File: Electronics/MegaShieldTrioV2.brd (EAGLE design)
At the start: 99.8 x 80 mm, 37 parts, among them X1 Vehicle control, X2 2odo__, X3 1odo__, X4 RJ45-8L-B, X5 S5B-ZR, X6 S6B-ZR, X7 22-23-2031

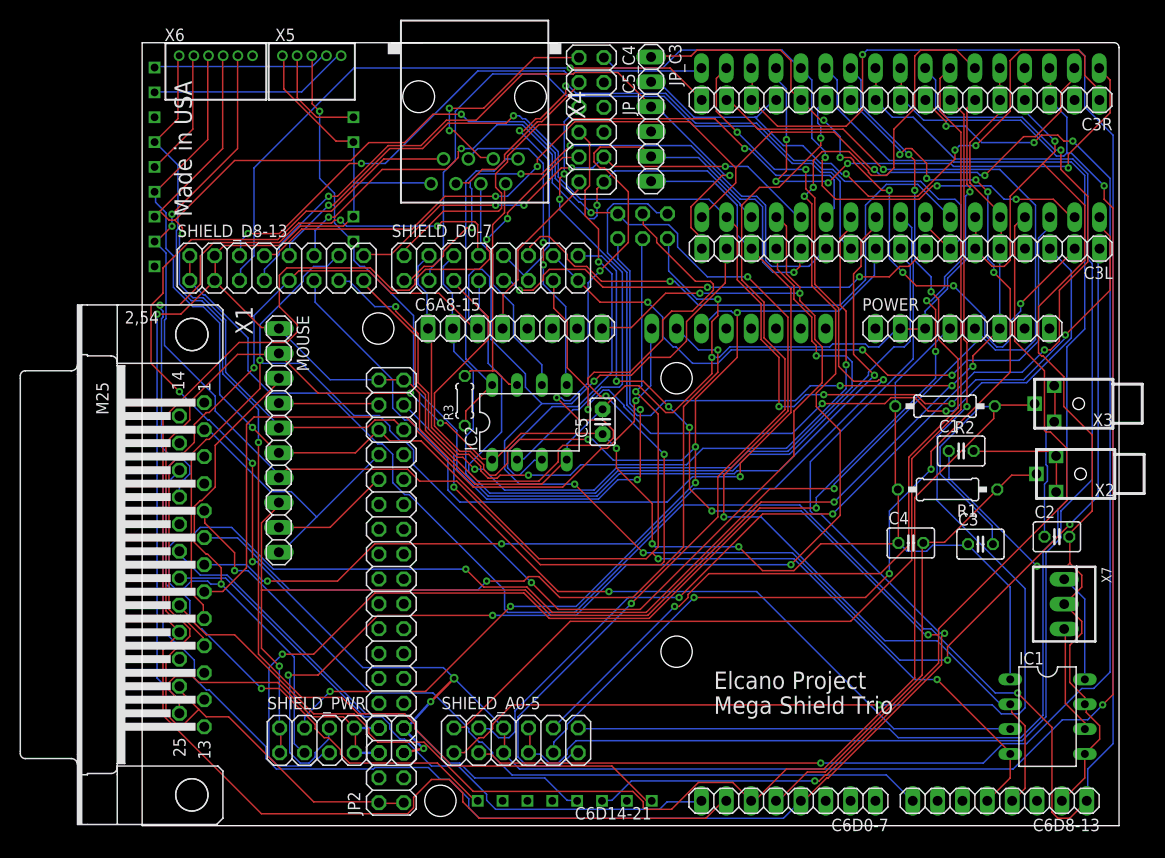
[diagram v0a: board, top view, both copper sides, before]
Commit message: Added four new boards to Electronics
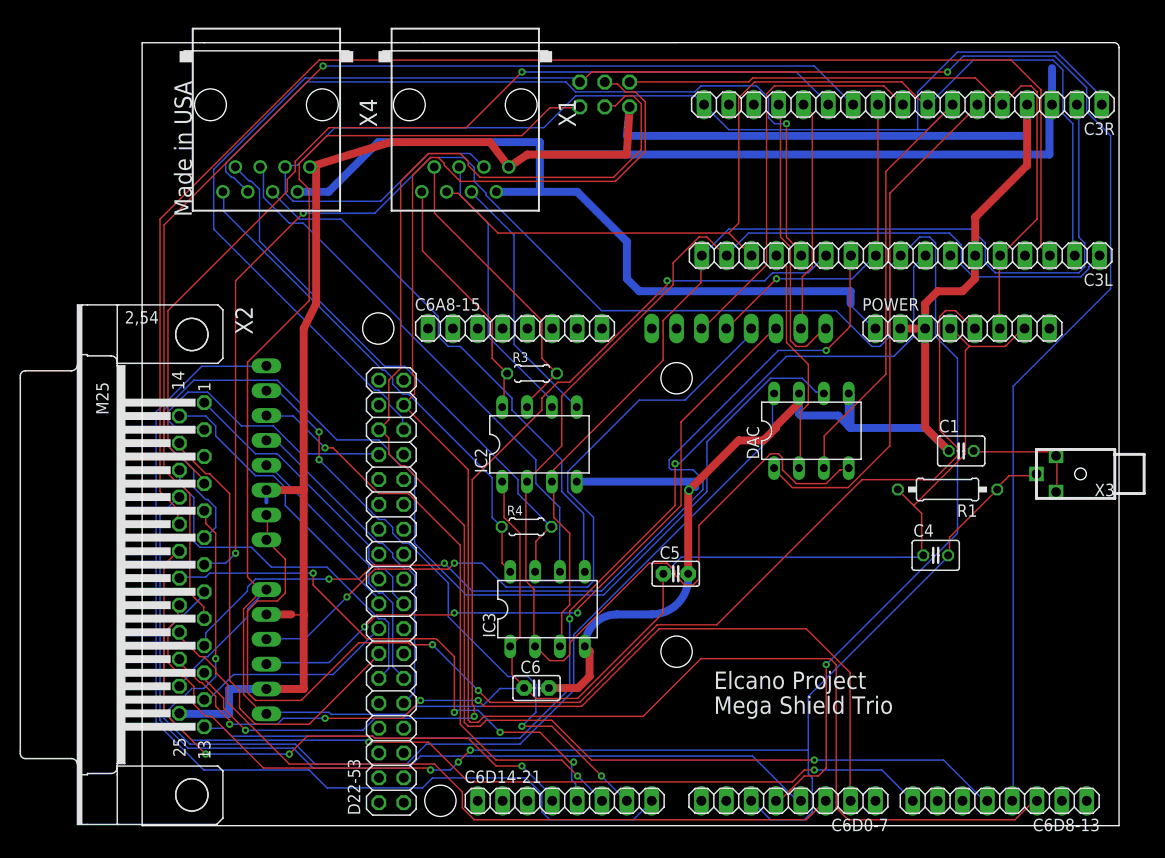
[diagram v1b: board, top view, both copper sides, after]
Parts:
- removed C2, C3: 1 uF, rcl:C025-030X050
- removed C4L, C4R: (no value), pinhead:1X17
- removed IC1: (no value), ic-package:DIL08
- removed INU: CHR_UM6, Elcano:CHR_UM6
- removed JP_C3: (no value), pinhead:1X06
- removed JP_C5_C4, SHIELD_A0-5, SHIELD_PWR: (no value), pinhead:2X06
- removed MOUSE: Visual odometry, pinhead:1X10
- removed R2: 4.7 K, rcl:0207/10
- removed SHIELD_D0-7, SHIELD_D8-13: (no value), pinhead:2X08
- removed X5: S5B-ZR, con-jst1:S5B-ZR
- removed X6: S6B-ZR, con-jst:S6B-ZR
- removed X7: 22-23-2031, con-molex:22-23-2031
- added C6: 0.1uF, capacitor-wima:C2.5-2
- added DAC: MCP 4802, ic-package:DIL08
- added IC3: DS 8291, ic-package:DIL08
- added JP3: Turns, pinhead:1X06
- added LSM303: (no value), pinhead:1X08
- added R4: 100, resistor:0204/5
- C3L: value (none) -> Pilot digital
- C3R: value (none) -> Pilot analog
- C6D14-21: value C6 Digital 14-21 -> GPS; device Elcano:1X8HEADER -> pinhead:1X08
- D22-53: value (none) -> High digital
- IC2: value (none) -> DS 8291
- X1: value Vehicle control -> RJ45-8L-B; device con-subd:M25H -> con-tycoelectronics:RJ45-NO-SHIELD
- X2: value 2odo__ -> Vehicle control; device Elcano:ODO_JACK -> con-subd:M25H
- X3: value 1odo__ -> 2odo__
- moved X2 91.3 mm to (5.08, 26.7), turned to 270 degrees
- moved X1 54.7 mm to (33.0, 73.7), turned to 180 degrees
- moved X4 21.3 mm to (12.7, 73.7)
- moved C5 17.2 mm to (54.5, 25.7), turned to 0 degrees
- moved ICSP 14.0 mm to (47.3, 74.7)
- moved C6D14-21 8.89 mm to (43.2, 2.54), turned to 0 degrees
- moved R3 7.42 mm to (39.8, 46.2), turned to 0 degrees
- moved X3 7.18 mm to (95.9, 35.9)
- moved C4 2.84 mm to (81.1, 27.6)
- moved IC2 2.48 mm to (40.6, 39.0)
- moved C3L 0.71 mm to (77.5, 58.3)
- moved C3R 0.53 mm to (77.7, 73.7)
- renumbered JP2 to D22-53
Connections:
- removed net 3.3V: C3R.16, MOUSE.3, POWER.5, SHIELD_PWR.3
- removed net 4D5_6A14: C4L.10, C6A8-15.2, SHIELD_D0-7.6
- removed net 4D6_6A15: C4L.11, C6A8-15.1, SHIELD_D0-7.4
- removed net 4D7_6D43: C4L.12, SHIELD_D0-7.2
- removed net 6D10_2A6: X1.23
- removed net AREF: C3R.15, C4R.15, C6D8-13.1, SHIELD_D8-13.1, SHIELD_D8-13.2
- removed net C2STAT: C6D14-21.P$4, X1.19
- removed net C4AVL: C3L.7, C4L.8, SHIELD_D0-7.10, SHIELD_D0-7.11
- removed net C4D12: C4L.17, C4R.2, SHIELD_D8-13.8
- removed net C6AVL: C4L.7, SHIELD_D0-7.12
- removed net C6D10: C6D8-13.6
- removed net CLICK1: C3.2, C6D0-7.6, R2.1, X1.21, X3.P$1
- removed net CLICK2: C4.2, C6D0-7.5, R1.1, X2.P$1
- removed net CRS_BRK: C3L.10, C6A0-7.6, SHIELD_D0-7.5, X1.7
- removed net CRS_STR: C6A0-7.7, X1.6
- removed net CRS_THR: C6A0-7.8, X1.8
- removed net D39: D22-53.20
- removed net D41: D22-53.22
- removed net DACA: IC1.8, X7.1
- removed net DACB: IC1.6, X7.3
- removed net DRV_CMD: X1.18
- removed net F2RNG: C4R.12, SHIELD_A0-5.12
- removed net FL_RNG: C4R.8, SHIELD_A0-5.4
- removed net GPS_CNTRL: C6D14-21.P$1, INU.D1, X6.1
- removed net GPS_LOC: C6D14-21.P$2
- removed net GPS_PPS: C6D14-21.P$7
- removed net GPS_PWR: C6D8-13.7
- removed net INU_BRN: C6D14-21.P$6
- removed net INU_CNTRL: C6D14-21.P$5
- removed net INU_SS: INU.D6
- removed net LED4: X1.3
- removed net L_RNG: C3R.10, C4R.10, SHIELD_A0-5.7, SHIELD_A0-5.8
- removed net MISO: C6D8-13.4, D22-53.31, IC1.2, ICSP.1, INU.D4, MOUSE.5, X6.4
- removed net MOSI: C6D8-13.5, D22-53.32, IC1.4, ICSP.4, INU.D3, MOUSE.6, X6.3
- removed net MOUSE_SS: D22-53.34, MOUSE.4
- removed net MOV_OK: C4L.9, C6D0-7.4, SHIELD_D0-7.8, X1.17
- removed net N$1: INU.3V, X5.2
- removed net N$11: C2.1, X3.P$2, X3.P$3
- removed net N$17: INU.RX, X5.5
- removed net N$2: INU.D2, X6.2
- removed net N$24: POWER.1
- removed net N$27: C4R.6, SHIELD_PWR.6
- removed net N$3: INU.TX, X5.4
- removed net N$36: C3R.17, SHIELD_D8-13.5
- removed net N$38: C3L.3, SHIELD_D0-7.13
- removed net N$39: ICSP.2, INU.VIN, X5.3
- removed net N$4: C3R.7, SHIELD_A0-5.1
- removed net N$40: C3R.6, SHIELD_PWR.5
- removed net N$41: C3L.8, SHIELD_D0-7.9
- removed net N$42: C3R.8, SHIELD_A0-5.3
- removed net N$45: C3R.11, SHIELD_A0-5.9
- removed net N$46: C3R.12, SHIELD_A0-5.11
- removed net N$47: C3R.1, C3R.14, JP_C3.2
- removed net N$48: C4R.1, C4R.14
- removed net N$49: C4R.11, SHIELD_A0-5.10
- removed net N$5: C4R.7, SHIELD_A0-5.2
- removed net N$51: C4R.17, SHIELD_D8-13.6
- removed net N$53: C3L.9, SHIELD_D0-7.7
- removed net N$54: C3L.11, SHIELD_D0-7.3
- removed net N$55: C3L.12, SHIELD_D0-7.1
- removed net N$57: C3L.14, SHIELD_D8-13.13
- removed net N$59: C3L.17, JP_C3.3, SHIELD_D8-13.7
- removed net N$6: X6.6
- removed net N$60: C3L.2, C3R.13, JP_C3.1
- removed net N$8: C4R.16, SHIELD_PWR.4
- removed net NAV_FIX: C4L.4, C6D14-21.P$3, SHIELD_D0-7.16
- removed net NPD: D22-53.28, MOUSE.9
- removed net PATH: C4L.3, SHIELD_D0-7.14, SHIELD_D0-7.15
- removed net SCK: ICSP.3, INU.D5, MOUSE.7, X6.5
- removed net SCLK: D22-53.33, IC1.3
- removed net SNR_SEL: C4L.2, C4R.13, JP_C5_C4.2
- removed net SNR_SO: C4L.1, C4L.16, SHIELD_D8-13.10
- removed net SPD_LMT: C4L.14, C6A8-15.8, SHIELD_D8-13.14, X1.9
- removed net SPEED: C3L.1, C3L.16, C6A8-15.3, SHIELD_D8-13.9, X1.10
- removed net SS2_3: C3L.13, JP_C3.5, SHIELD_D8-13.15
- removed net SS2_3/4: C6D0-7.7, JP_C5_C4.9, X1.22
- removed net SS2_4: C4L.13, JP_C5_C4.10, SHIELD_D8-13.16
- removed net SS3/4_6: C6A8-15.4, JP_C5_C4.11
- removed net SS3_6: C3L.15, JP_C3.6, SHIELD_D8-13.11
- removed net SS4_2: C6D0-7.8, X1.20
- removed net SS4_6: C4L.15, JP_C5_C4.12, SHIELD_D8-13.12
- removed net S_SCK: JP_C5_C4.3, X4.6
- removed net S_SI: IC2.2, JP_C5_C4.5
- removed net S_SO: IC2.3, JP_C5_C4.7
- removed net S_SS: JP_C5_C4.1, X4.3
- new net 2TX6RX: C6D14-21.4, X2.19
- new net 3MISO: C3L.17, C3R.2, IC2.3, IC3.3
- new net 3MOSI: C3L.1, C3L.16, DAC.4, IC2.2, IC3.2
- new net 3SCK: C3R.1, C3R.17, C3R.7, DAC.3, X1.3, X4.3
- new net 3SS5F: C3L.15, C3L.2, C3R.8, X1.6
- new net 3SS5R: C3L.13, X4.6
- new net 3SS_DAC: C3L.14, DAC.2
- new net 3TX2RX: C3L.3, X2.18
- new net 3V3: LSM303.1, LSM303.2, POWER.5
- new net 5V_C3: C3R.6, DAC.1
- new net 6MISO: C6D8-13.4, D22-53.31, ICSP.1
- new net 6MOSI: C6D8-13.5, D22-53.32, ICSP.4
- new net 6SCK: C6D8-13.3, D22-53.33, ICSP.3
- new net 6SCL: C6D14-21.8, LSM303.8
- new net 6SDA: C6D14-21.7, LSM303.7
- new net 6TX2RX: C6D14-21.5, X2.20
- new net A0: C3R.14, C6A0-7.1
- new net A1: C3R.13, C6A0-7.2
- new net A5: C3R.9, C6A0-7.6
- new net ACK26: C6D0-7.4, X2.17
- new net ACK34: C3R.11, X2.9
- new net ACK43: C3L.10, C3R.10, C6A0-7.5
- new net ACK62: C6D0-7.3, X2.22
- new net AUTREQ: C3L.9, C6D0-7.5, X2.7
- new net CLICK: C4.2, C6D0-7.6, R1.1, X2.21, X3.P$1
- new net CRSSTR: DAC.6, X2.6
- new net CRSTHR: DAC.8, X2.8
- new net D09: D22-53.18, X2.14
- new net DRDY: D22-53.11, LSM303.4
- new net I1LSM: C6D14-21.6, LSM303.6
- new net I2LSM: D22-53.9, LSM303.5
- new net MANRQ: C3L.11, X2.10
- new net MISO+R: IC3.6, X4.5
- new net MISO-R: IC3.5, X4.4
- new net MOSI+R: IC3.8, R4.1, X4.8
- new net MOSI-R: IC3.7, R4.2, X4.7
- new net RDY26: D22-53.16, X2.12
- new net RDY32: C3L.12, X2.11
- new net RDY62: C6D0-7.2, X2.23
- new net STR_L: C6A0-7.3, JP3.3
- new net STR_R: C6A0-7.4, JP3.4
- net +5V: now also C6.1, IC3.1, ICSP.2, JP3.1, JP3.6, POWER.7, X2.24; no longer C3.1, D22-53.1, D22-53.2, IC1.1, MOUSE.2, R2.2, X1.24
- net CRS_RVS: now also C3L.8, X2.13; no longer X1.13
- net GND: now also C6.2, DAC.5, DAC.7, IC3.4, JP3.2, JP3.5, LSM303.3, X1.1, X2.25, X4.1; no longer C2.2, C4L.6, C4R.4, C6D8-13.2, D22-53.35, D22-53.36, IC1.5, IC1.7, INU.GND, INU.GND2, MOUSE.1, SHIELD_D8-13.3, SHIELD_D8-13.4, SHIELD_PWR.10, SHIELD_PWR.7, SHIELD_PWR.8, SHIELD_PWR.9, X1.25, X4.8, X5.1, X7.2
- net LED1: now also X2.5; no longer X1.5
- net LED3: now also C3R.12, X2.4; no longer X1.4
- net LED5: now also X2.2; no longer MOUSE.10, X1.2
- net LED6: now also D22-53.17, X2.1; no longer X1.1
- net LED7: now also D22-53.14, X2.15; no longer X1.15
- net LED8: now also D22-53.12, X2.16; no longer C6D14-21.P$8, X1.16
- net MISO+: now also X1.5; no longer X4.4
- net MISO-: now also X1.4; no longer X4.5
- net MOSI+: now also X1.8; no longer X4.1
- net MOSI-: now also X1.7; no longer X4.2
- net N$23: now also X3.P$2, X3.P$3; no longer X2.P$2, X2.P$3
- net RESET: no longer C4L.5, C4R.5, MOUSE.8, SHIELD_PWR.1, SHIELD_PWR.2
- net VIN: now also POWER.1, X1.2, X4.2; no longer C3R.9, C4R.3, C4R.9, SHIELD_A0-5.5, SHIELD_A0-5.6, SHIELD_PWR.11, SHIELD_PWR.12, X4.7
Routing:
- net AREF: track 260.4 -> 0.00 mm, vias 2 -> 0
- net MOV_OK: track 235.0 -> 0.00 mm, vias 4 -> 0
- net SPEED: track 229.1 -> 0.00 mm, vias 6 -> 0
- net 3.3V: track 214.4 -> 0.00 mm, vias 4 -> 0
- net MISO: track 211.0 -> 0.00 mm, vias 5 -> 0
- net 6MISO: track 0.00 -> 208.6 mm, vias 0 -> 1
- net AUTREQ: track 0.00 -> 192.9 mm, vias 0 -> 3
- net MOSI: track 178.3 -> 0.00 mm, vias 4 -> 0
- net 6SCK: track 0.00 -> 173.1 mm
- net 3SCK: track 0.00 -> 169.3 mm
- net SPD_LMT: track 167.0 -> 0.00 mm, vias 4 -> 0
- net SS2_3/4: track 162.1 -> 0.00 mm, vias 2 -> 0
- net NAV_FIX: track 157.3 -> 0.00 mm, vias 6 -> 0
- net 6MOSI: track 0.00 -> 154.9 mm, vias 0 -> 1
- net CRS_BRK: track 148.4 -> 0.00 mm, vias 6 -> 0
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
